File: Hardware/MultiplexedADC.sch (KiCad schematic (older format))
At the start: 9 parts, among them J15 Alert, U11 V-Shift, U8 MUX, U9 ADC

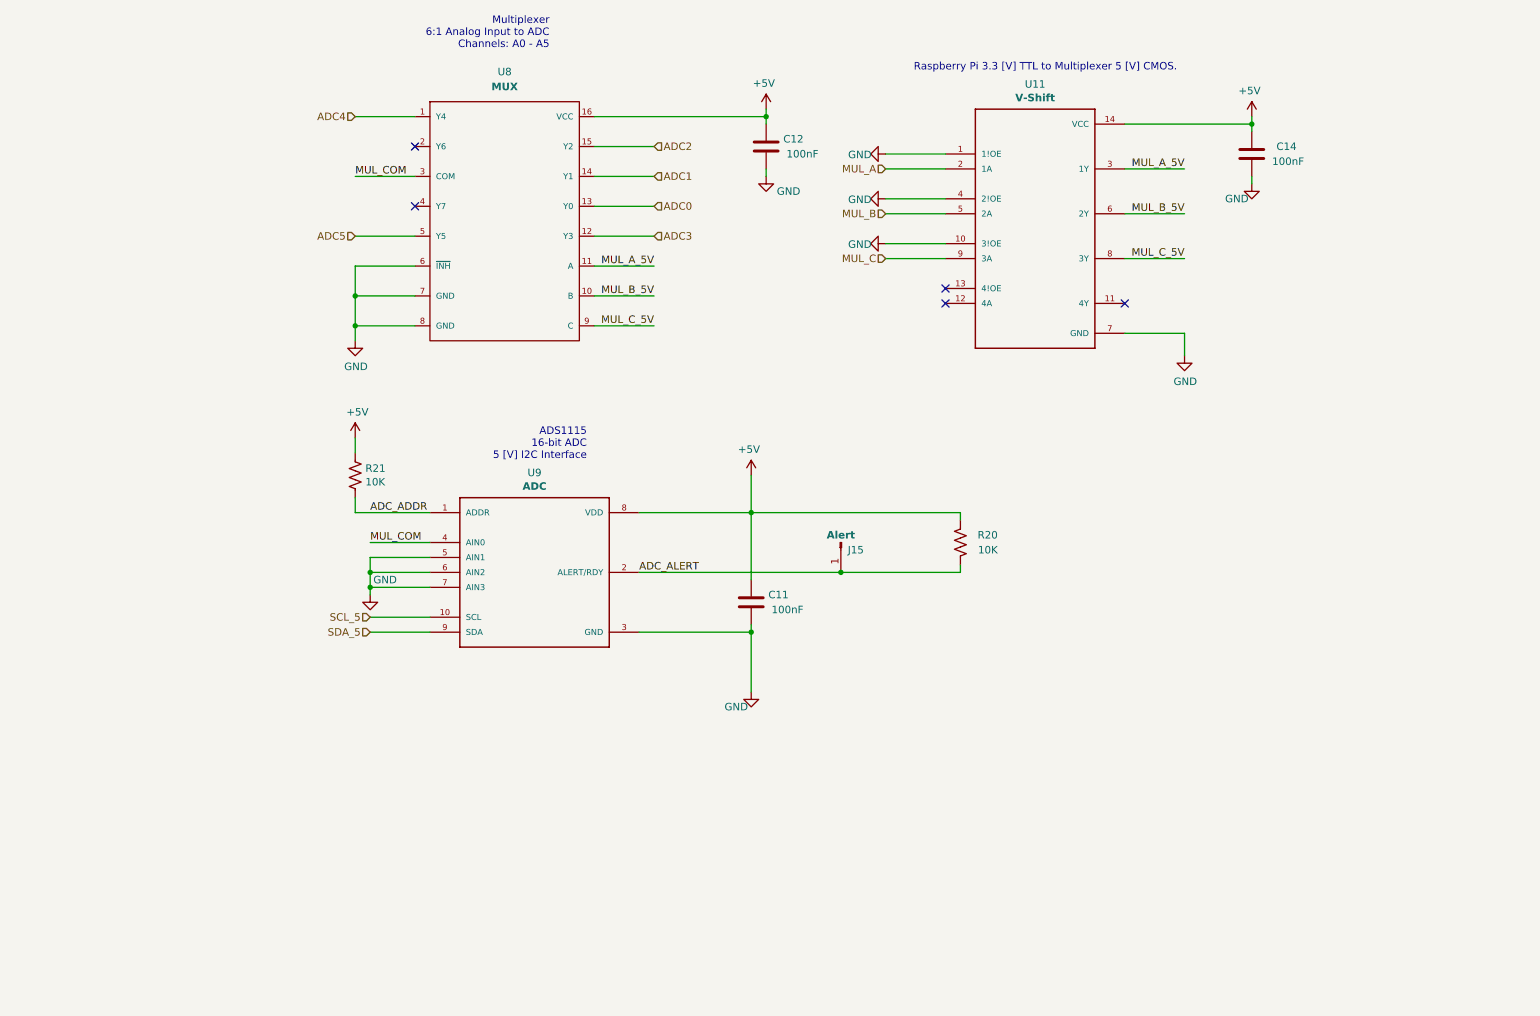
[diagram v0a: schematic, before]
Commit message: Organized Schematic Naming and Added Comments
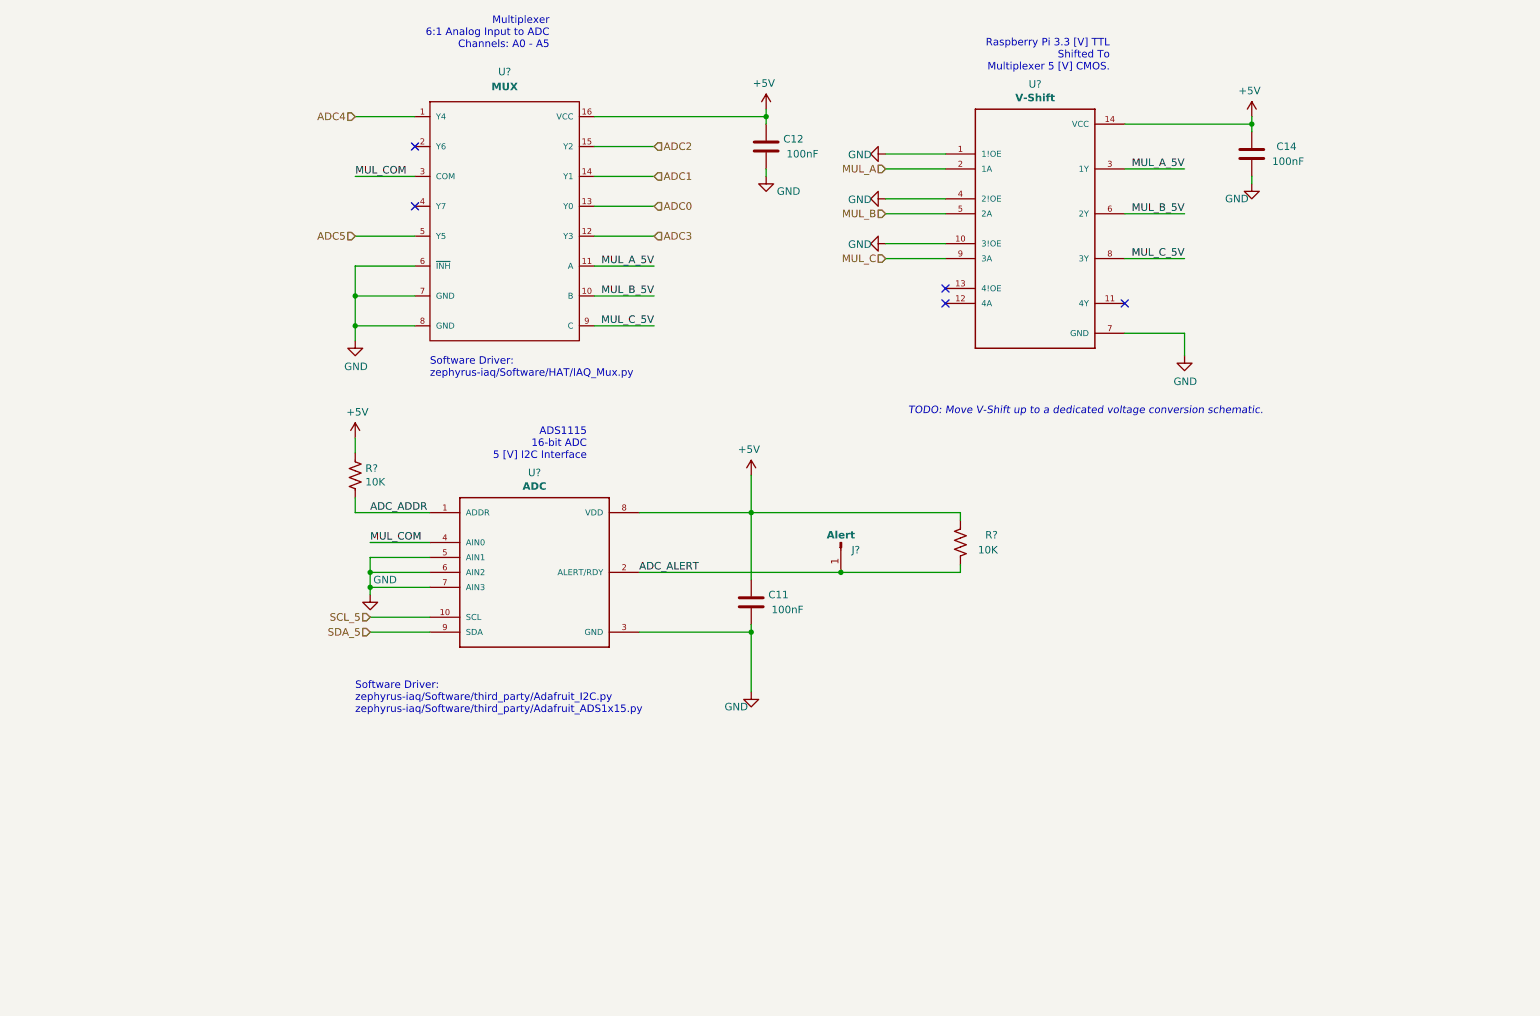
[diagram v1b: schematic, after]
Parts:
- renumbered J15 to J?, R20 to R?, R21 to R?, U11 to U?, U9 to U?, U8 to U?
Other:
- note added: "Raspberry Pi 3.3 [V] TTL\nShifted To\n Multiplexer 5 [V] CMOS."
- note added: "Software Driver:\nzephyrus-iaq/Software/HAT/IAQ_Mux.py"
- note added: "Software Driver:\nzephyrus-iaq/Software/third_party/Adafruit_I2C.py\nzephyrus-iaq/Software/third_party/Adafruit_ADS1x15.py"
- note added: "TODO: Move V-Shift up to a dedicated voltage conversion schematic."
- note removed: "Raspberry Pi 3.3 [V] TTL to Multiplexer 5 [V] CMOS."
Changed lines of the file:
@@
 EESchema Schematic File Version 4
-LIBS:rpi-hat-cache
+LIBS:TopLevel-cache
 EELAYER 30 0
 EELAYER END
@@
 encoding utf-8
 Sheet 2 7
-Title ""
-Date ""
+Title "Multiplexed Analog Input"
+Date "2019-11-15"
 Rev ""
-Comp ""
+Comp "Zephyrus, Indoor Air Quality - Raspberry Pi HAT"
 Comment1 ""
 Comment2 ""
@@
 $EndDescr
 $Comp
-L zephyrus_iaq:ADS1115IDGSR U9
+L zephyrus_iaq:ADS1115IDGSR U?
 U 1 1 5DAF67B5
 P 4100 5250
-F 0 "U9" H 4100 5917 50  0000 C CNN
+F 0 "U?" H 4100 5917 50  0000 C CNN
 F 1 "ADC" H 4100 5826 50  0000 C CNB
 F 2 "zephyrus-iaq:SOP50P490X110-10N" H 3800 6350 50  0001 L BNN
@@
 SDA_5
 $Comp
-L zephyrus_iaq:SN74lV4051A U8
+L zephyrus_iaq:SN74lV4051A U?
 U 1 1 5DB1D523
 P 3900 2100
-F 0 "U8" H 3900 2300 50  0000 C CNN
+F 0 "U?" H 3900 2300 50  0000 C CNN
 F 1 "MUX" H 3900 2200 50  0000 C CNB
 F 2 "zephyrus-iaq:SOP65P640X120-16N" H 3900 2100 50  0001 C CNN
@@
 $EndComp
 $Comp
-L zephyrus_iaq:GND #PWR059
+L zephyrus_iaq:GND #PWR?
 U 1 1 5DB2199F
 P 3000 5400
-F 0 "#PWR059" H 3000 5150 50  0001 C CNN
+F 0 "#PWR?" H 3000 5150 50  0001 C CNN
 F 1 "GND" H 3100 5500 50  0000 C CNN
 F 2 "" H 3000 5400 50  0001 C CNN
@@
 	3300 3600 2900 3600
 $Comp
-L zephyrus_iaq:GND #PWR061
+L zephyrus_iaq:GND #PWR?
 U 1 1 5DB26E25
 P 2900 3700
-F 0 "#PWR061" H 2900 3450 50  0001 C CNN
+F 0 "#PWR?" H 2900 3450 50  0001 C CNN
 F 1 "GND" H 2905 3527 50  0000 C CNN
 F 2 "" H 2900 3700 50  0001 C CNN
@@
 	3000 5650 3400 5650
 $Comp
-L zephyrus_iaq:Conn_01x01_Male J15
+L zephyrus_iaq:Conn_01x01_Male J?
 U 1 1 5DB74FAD
 P 6150 5050
-F 0 "J15" V 6200 4950 50  0000 C CNN
+F 0 "J?" V 6200 4950 50  0000 C CNN
 F 1 "Alert" V 6100 5050 50  0000 C CNB
 F 2 "zephyrus-iaq:PinHeader_1x01_P2.54mm_Vertical" H 6150 5050 50  0001 C CNN
@@
 $EndComp
 $Comp
-L zephyrus_iaq:R_US R21
+L zephyrus_iaq:R_US R?
 U 1 1 5DB93A1B
 P 2900 4600
-F 0 "R21" H 2968 4646 50  0000 L CNN
+F 0 "R?" H 2968 4646 50  0000 L CNN
 F 1 "10K" H 2968 4555 50  0000 L CNN
 F 2 "Resistor_SMD:R_0805_2012Metric" V 2940 4590 50  0001 C CNN
@@
 ADC4
 $Comp
-L zephyrus_iaq:SN74LV4T125PWR U11
+L zephyrus_iaq:SN74LV4T125PWR U?
 U 1 1 5D9F68B4
 P 7450 2950
-F 0 "U11" H 7450 3917 50  0000 C CNN
+F 0 "U?" H 7450 3917 50  0000 C CNN
 F 1 "V-Shift" H 7450 3826 50  0000 C CNB
 F 2 "zephyrus-iaq:SOP65P640X120-14N" H 7450 2950 50  0001 L BNN
@@
 	8450 3650 8050 3650
 $Comp
-L zephyrus_iaq:GND #PWR0109
+L zephyrus_iaq:GND #PWR?
 U 1 1 5DA06364
 P 6450 2450
-F 0 "#PWR0109" H 6450 2200 50  0001 C CNN
+F 0 "#PWR?" H 6450 2200 50  0001 C CNN
 F 1 "GND" V 6455 2277 50  0000 C CNN
 F 2 "" H 6450 2450 50  0001 C CNN
@@
 $EndComp
 $Comp
-L zephyrus_iaq:GND #PWR0110
+L zephyrus_iaq:GND #PWR?
 U 1 1 5DA0782E
 P 6450 2750
-F 0 "#PWR0110" H 6450 2500 50  0001 C CNN
+F 0 "#PWR?" H 6450 2500 50  0001 C CNN
 F 1 "GND" V 6455 2577 50  0000 C CNN
 F 2 "" H 6450 2750 50  0001 C CNN
@@
 $EndComp
 $Comp
-L zephyrus_iaq:GND #PWR0111
+L zephyrus_iaq:GND #PWR?
 U 1 1 5DA08CD6
 P 6450 3050
-F 0 "#PWR0111" H 6450 2800 50  0001 C CNN
+F 0 "#PWR?" H 6450 2800 50  0001 C CNN
 F 1 "GND" V 6455 2877 50  0000 C CNN
 F 2 "" H 6450 3050 50  0001 C CNN
@@
 	4500 3600 4900 3600
 $Comp
-L zephyrus_iaq:GND #PWR0113
+L zephyrus_iaq:GND #PWR?
 U 1 1 5DA136A6
 P 8450 3800
-F 0 "#PWR0113" H 8450 3550 50  0001 C CNN
+F 0 "#PWR?" H 8450 3550 50  0001 C CNN
 F 1 "GND" H 8455 3627 50  0000 C CNN
 F 2 "" H 8450 3800 50  0001 C CNN
@@
 	6950 5250 6150 5250
 $Comp
-L zephyrus_iaq:R_US R20
+L zephyrus_iaq:R_US R?
 U 1 1 5DB7485C
 P 6950 5050
-F 0 "R20" H 6700 5100 50  0000 L CNN
+F 0 "R?" H 6700 5100 50  0000 L CNN
 F 1 "10K" H 6700 5000 50  0000 L CNN
 F 2 "Resistor_SMD:R_0805_2012Metric" V 6990 5040 50  0001 C CNN
@@
 Text Notes 4200 1750 2    50   ~ 0
 Multiplexer\n6:1 Analog Input to ADC\nChannels: A0 - A5\n
-Text Notes 8400 1900 2    50   ~ 0
-Raspberry Pi 3.3 [V] TTL to Multiplexer 5 [V] CMOS.
+Text Notes 7950 1900 2    50   ~ 0
+Raspberry Pi 3.3 [V] TTL\nShifted To\n Multiplexer 5 [V] CMOS.
 Text Notes 4450 4500 2    50   ~ 0
 ADS1115\n16-bit ADC\n5 [V] I2C Interface
@@
 Wire Wire Line
 	5550 4850 5550 5300
+Text Notes 2900 6200 0    50   ~ 0
+Software Driver:\nzephyrus-iaq/Software/third_party/Adafruit_I2C.py\nzephyrus-iaq/Software/third_party/Adafruit_ADS1x15.py
+Text Notes 3400 3950 0    50   ~ 0
+Software Driver:\nzephyrus-iaq/Software/HAT/IAQ_Mux.py
+Text Notes 6600 4200 0    50   Italic 0
+TODO: Move V-Shift up to a dedicated voltage conversion schematic.
 $EndSCHEMATC

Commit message: Up Changed I2C addres for DAC and ADC.  Added MOSFET to USART RX.
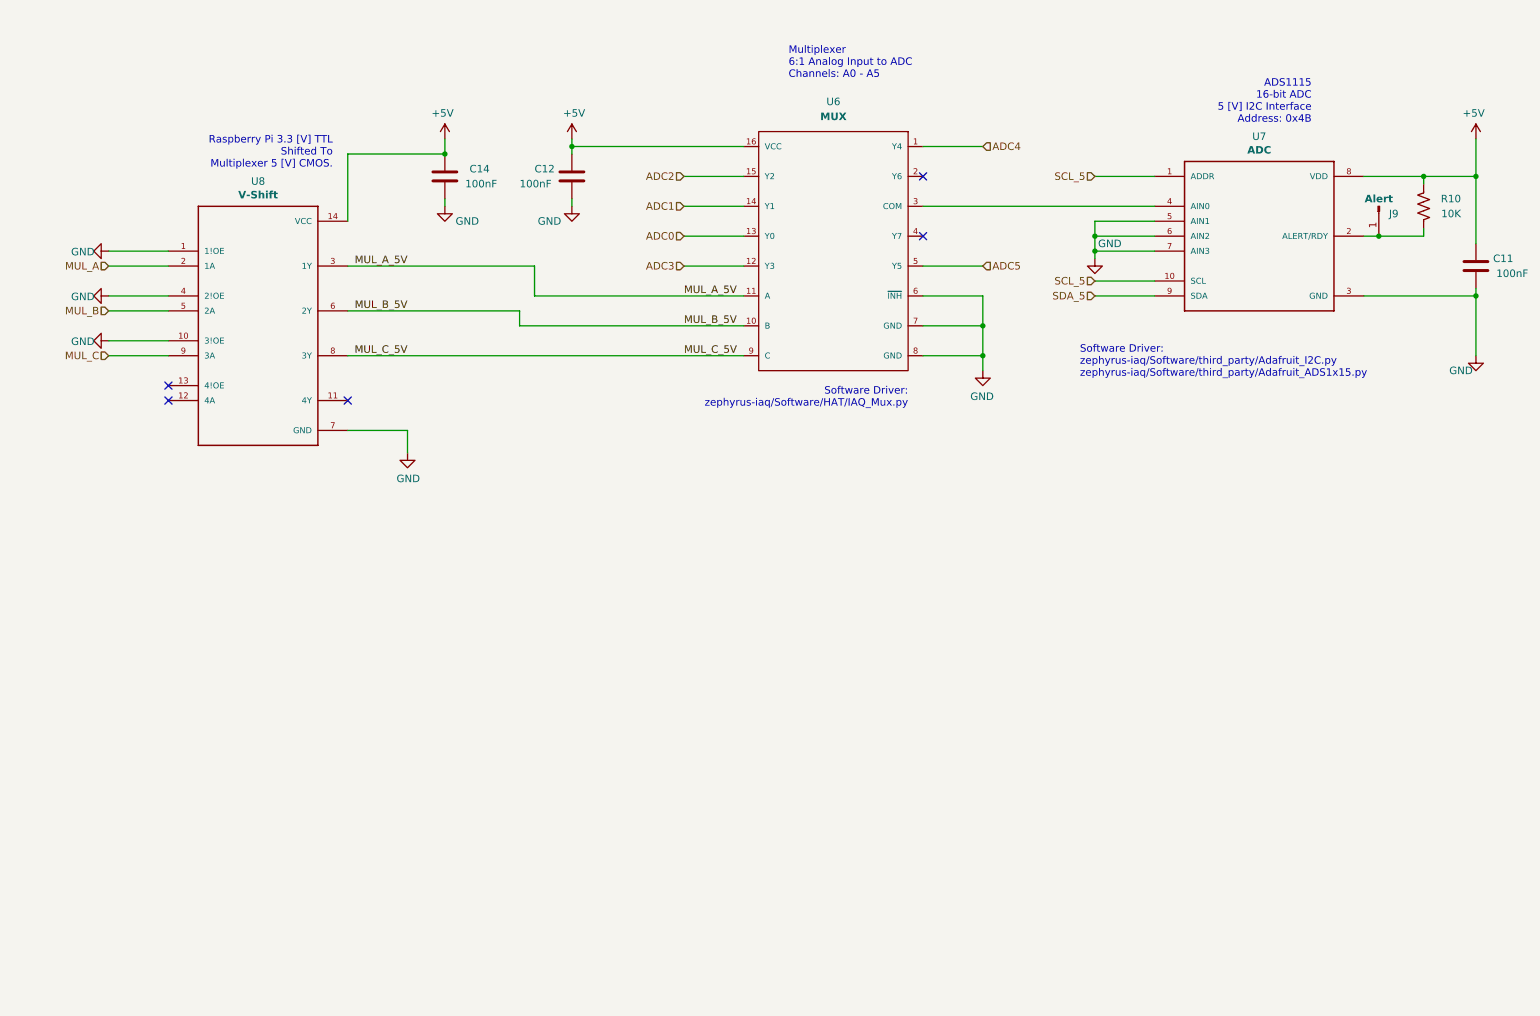
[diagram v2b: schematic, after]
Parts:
- removed R?: 10K, Resistor_SMD:R_0805_2012Metric, symbol zephyrus_iaq:R_US
- gave numbers to parts that had none: 5
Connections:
- net ADC_ADDR is gone; now on net SCL_5: U7.1 (ADDR)
- net ADC_ALERT: no longer names the net of J9.1 (Pin_1), R10.2, U7.2 (ALERT/RDY)
- net MUL_COM: no longer names the net of U6.3 (COM), U7.4 (AIN0)
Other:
- note added: "ADS1115\n16-bit ADC\n5 [V] I2C Interface\nAddress: 0x4B"
- note removed: "ADS1115\n16-bit ADC\n5 [V] I2C Interface"
- note removed: "TODO: Move V-Shift up to a dedicated voltage conversion schematic."
- moved on the sheet: C11, C12, C14, J9, R10, U6, U7, U8

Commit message: Updated Schematic Attribution and Documentation
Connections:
- wire segments 56 -> 57
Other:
- note added: "ADS1115\n16-bit ADC\n5 [V] I2C Interface"
- note added: "Address: 0x4B"
- note removed: "ADS1115\n16-bit ADC\n5 [V] I2C Interface\nAddress: 0x4B"
- moved on the sheet: C11, C12, C14, J9, R10, U6, U7, U8
